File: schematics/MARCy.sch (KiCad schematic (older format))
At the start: 2 parts, among them J2 JTAG, U3 XC9572XL-TQ100

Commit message: merge from Jani's commit
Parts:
- added R?: 0.1uF, symbol Device:R_Small
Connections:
- net GND: now also R?.2
- net Vcc33: now also R?.1
- net A0: now reaches U3.32 (P32)
- net R~W: now reaches U3.33 (P33)
- net A1: now reaches U3.35 (P35)
- net ~OE: now reaches U3.36 (P36)
- net A2: now reaches U3.37 (P37)
- net A3: now reaches U3.41 (P41)
- net A4: now reaches U3.42 (P42)
- net A5: now reaches U3.49 (P49)
- net A6: now reaches U3.50 (P50)
- net A7: now reaches U3.52 (P52)
- net A8: now reaches U3.53 (P53)
- net A9: now reaches U3.54 (P54)
- net A10: now reaches U3.55 (P55)
- net A11: now reaches U3.56 (P56)
- net A12: now reaches U3.58 (P58)
- net A13: now reaches U3.59 (P59)
- net A14: now reaches U3.60 (P60)
- net A15: now reaches U3.61 (P61)
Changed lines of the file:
@@
 Connection ~ 4150 6650
 Entry Wire Line
-	5350 2050 5450 1950
-Entry Wire Line
-	5350 2150 5450 2050
-Entry Wire Line
-	5350 2250 5450 2150
-Entry Wire Line
-	5350 2350 5450 2250
-Entry Wire Line
-	5350 2450 5450 2350
-Entry Wire Line
-	5350 2550 5450 2450
-Entry Wire Line
-	5350 2650 5450 2550
-Entry Wire Line
-	5350 2750 5450 2650
-Entry Wire Line
-	5350 2850 5450 2750
-Entry Wire Line
-	5350 2950 5450 2850
-Entry Wire Line
-	5350 3050 5450 2950
-Entry Wire Line
-	5350 3150 5450 3050
-Entry Wire Line
-	5350 3250 5450 3150
-Entry Wire Line
-	5350 3350 5450 3250
-Entry Wire Line
-	5350 3450 5450 3350
-Entry Wire Line
-	5350 3550 5450 3450
-Text Label 5450 1350 0    50   ~ 10
-A[0..15]
-Text GLabel 5450 1600 2    50   Input ~ 10
-A[0..15]
-Text GLabel 2450 2050 0    50   Input ~ 10
+	5500 2050 5600 1950
+Entry Wire Line
+	5500 2150 5600 2050
+Entry Wire Line
+	5500 2250 5600 2150
+Entry Wire Line
+	5500 2350 5600 2250
+Entry Wire Line
+	5500 2450 5600 2350
+Entry Wire Line
+	5500 2550 5600 2450
+Entry Wire Line
+	5500 2650 5600 2550
+Entry Wire Line
+	5500 2750 5600 2650
+Entry Wire Line
+	5500 2850 5600 2750
+Entry Wire Line
+	5500 2950 5600 2850
+Entry Wire Line
+	5500 3050 5600 2950
+Entry Wire Line
+	5500 3150 5600 3050
+Entry Wire Line
+	5500 3250 5600 3150
+Entry Wire Line
+	5500 3350 5600 3250
+Entry Wire Line
+	5500 3450 5600 3350
+Entry Wire Line
+	5500 3550 5600 3450
+Text GLabel 2450 2050 0    50   Output ~ 10
 RTC_EN
-Text GLabel 2450 2200 0    50   Input ~ 10
+Text GLabel 2450 2200 0    50   Output ~ 10
 VIA1_EN
 Wire Wire Line
@@
 Wire Wire Line
 	3050 2150 3050 2200
-Text GLabel 2450 2350 0    50   Input ~ 10
+Text GLabel 2450 2350 0    50   Output ~ 10
 VIA2_EN
 Wire Wire Line
@@
 Wire Wire Line
 	3100 2250 3100 2350
-Text GLabel 2450 2500 0    50   Input ~ 10
+Text GLabel 2450 2500 0    50   Output ~ 10
 ROM_EN
 Wire Wire Line
@@
 Wire Wire Line
 	2600 2500 2450 2500
-Text GLabel 2450 2650 0    50   Input ~ 10
+Text GLabel 2450 2650 0    50   Output ~ 10
 RAM_EN
 Wire Wire Line
 	2650 2650 2450 2650
-Text GLabel 2450 2800 0    50   Input ~ 10
+Text GLabel 2450 2800 0    50   Output ~ 10
 UART_EN
-Text GLabel 2400 2950 0    50   Input ~ 10
+Text GLabel 2400 2950 0    50   Output ~ 10
 GRACE_EN
 Wire Wire Line
@@
 Wire Wire Line
 	2400 2950 2750 2950
-Text GLabel 2350 3100 0    50   Input ~ 10
+Text GLabel 2350 3100 0    50   Output ~ 10
 CAS
 Wire Wire Line
@@
 Wire Wire Line
 	2800 3100 2350 3100
-Text GLabel 2350 3250 0    50   Input ~ 10
+Text GLabel 2350 3250 0    50   Output ~ 10
 RAS
 Wire Wire Line
@@
 Wire Wire Line
 	2500 3250 2350 3250
-Text GLabel 2350 3400 0    50   Input ~ 10
+Text GLabel 2350 3400 0    50   Output ~ 10
 AUDIO_EN
 Wire Wire Line
@@
 Wire Wire Line
 	5950 6050 5350 6050
-Text GLabel 5400 750  2    50   Input ~ 10
-Vcc33
 Wire Wire Line
 	4650 750  5400 750
@@
 	6950 5400 5800 5400
 Entry Wire Line
-	5350 3950 5450 3850
-Entry Wire Line
-	5350 4050 5450 3950
-Entry Wire Line
-	5350 4150 5450 4050
-Entry Wire Line
-	5350 4250 5450 4150
-Entry Wire Line
-	5350 4350 5450 4250
-Entry Wire Line
-	5350 4450 5450 4350
-Entry Wire Line
-	5350 4550 5450 4450
-Entry Wire Line
-	5350 4650 5450 4550
-Entry Wire Line
-	5350 4750 5450 4650
-Entry Wire Line
-	5350 4850 5450 4750
-Entry Wire Line
-	5350 4950 5450 4850
-Entry Wire Line
-	5350 5050 5450 4950
-Text Label 5450 4100 0    50   ~ 10
+	5500 3950 5600 3850
+Entry Wire Line
+	5500 4050 5600 3950
+Entry Wire Line
+	5500 4150 5600 4050
+Entry Wire Line
+	5500 4250 5600 4150
+Entry Wire Line
+	5500 4350 5600 4250
+Entry Wire Line
+	5500 4450 5600 4350
+Entry Wire Line
+	5500 4550 5600 4450
+Entry Wire Line
+	5500 4650 5600 4550
+Entry Wire Line
+	5500 4750 5600 4650
+Entry Wire Line
+	5500 4850 5600 4750
+Entry Wire Line
+	5500 4950 5600 4850
+Entry Wire Line
+	5500 5050 5600 4950
+Text GLabel 2350 3550 0    50   Output ~ 10
+FDC_EN
+Wire Wire Line
+	3350 3350 2600 3350
+Wire Wire Line
+	2600 3350 2600 3550
+Wire Wire Line
+	2600 3550 2350 3550
+Wire Wire Line
+	5350 2050 5500 2050
+Wire Wire Line
+	5350 2150 5500 2150
+Wire Wire Line
+	5350 2250 5500 2250
+Wire Wire Line
+	5350 2350 5500 2350
+Wire Wire Line
+	5350 2450 5500 2450
+Wire Wire Line
+	5350 2550 5500 2550
+Wire Wire Line
+	5350 2650 5500 2650
+Wire Wire Line
+	5350 2750 5500 2750
+Wire Wire Line
+	5350 2850 5500 2850
+Wire Wire Line
+	5350 2950 5500 2950
+Wire Wire Line
+	5350 3050 5500 3050
+Wire Wire Line
+	5350 3150 5500 3150
+Wire Wire Line
+	5350 3250 5500 3250
+Wire Wire Line
+	5350 3350 5500 3350
+Wire Wire Line
+	5350 3450 5500 3450
+Wire Wire Line
+	5350 3550 5500 3550
+Wire Bus Line
+	5600 1950 5700 1950
+Text Label 5350 2050 0    50   ~ 0
+A0
+Text Label 5350 2150 0    50   ~ 0
+A1
+Text Label 5350 2250 0    50   ~ 0
+A2
+Text Label 5350 2350 0    50   ~ 0
+A3
+Text Label 5350 2450 0    50   ~ 0
+A4
+Text Label 5350 2550 0    50   ~ 0
+A5
+Text Label 5350 2650 0    50   ~ 0
+A6
+Text Label 5350 2750 0    50   ~ 0
+A7
+Text Label 5350 2850 0    50   ~ 0
+A8
+Text Label 5350 2950 0    50   ~ 0
+A9
+Text Label 5350 3050 0    50   ~ 0
+A10
+Text Label 5350 3150 0    50   ~ 0
+A11
+Text Label 5350 3250 0    50   ~ 0
+A12
+Text Label 5350 3350 0    50   ~ 0
+A13
+Text Label 5350 3450 0    50   ~ 0
+A14
+Text Label 5350 3550 0    50   ~ 0
+A15
+Wire Wire Line
+	5350 3950 5500 3950
+Wire Wire Line
+	5350 4050 5500 4050
+Wire Wire Line
+	5350 4150 5500 4150
+Wire Wire Line
+	5350 4250 5500 4250
+Wire Wire Line
+	5350 4350 5500 4350
+Wire Wire Line
+	5350 4450 5500 4450
+Wire Wire Line
+	5350 4550 5500 4550
+Wire Wire Line
+	5350 4650 5500 4650
+Wire Wire Line
+	5350 4750 5500 4750
+Wire Wire Line
+	5350 4850 5500 4850
+Wire Wire Line
+	5350 4950 5500 4950
+Wire Wire Line
+	5350 5050 5500 5050
+Wire Bus Line
+	5600 3850 5650 3850
+Text HLabel 5650 3850 2    50   Output ~ 0
 MA[0..11]
-Text GLabel 5450 4300 2    50   Input ~ 10
-MA[0..11]
-Text GLabel 2350 3550 0    50   Input ~ 10
-FDC_EN
-Wire Wire Line
-	3350 3350 2600 3350
-Wire Wire Line
-	2600 3350 2600 3550
-Wire Wire Line
-	2600 3550 2350 3550
+Text HLabel 5700 1950 2    50   Input ~ 0
+A[0..15]
+Text HLabel 7300 1000 0    50   Input ~ 0
+Vcc33
+$Comp
+L Device:R_Small R?
+U 1 1 5F14E0B3
+P 7450 1100
+F 0 "R?" H 7509 1146 50  0000 L CNN
+F 1 "0.1uF" H 7509 1055 50  0000 L CNN
+F 2 "" H 7450 1100 50  0001 C CNN
+F 3 "~" H 7450 1100 50  0001 C CNN
+	1    7450 1100
+	1    0    0    -1
+$EndComp
+Wire Wire Line
+	7300 1000 7450 1000
+Wire Wire Line
+	7450 1000 7800 1000
+Connection ~ 7450 1000
+Text HLabel 7300 1200 0    50   Input ~ 0
+GND
+Text GLabel 7800 1000 2    50   Output ~ 0
+Vcc33
+Text GLabel 7800 1200 2    50   Output ~ 0
+GND
+Wire Wire Line
+	7800 1200 7450 1200
+Wire Wire Line
+	7300 1200 7450 1200
+Connection ~ 7450 1200
+Text GLabel 5400 750  2    50   Input ~ 0
+Vcc33
+Text HLabel 2300 3750 0    50   Input ~ 0
+R~W
+Text HLabel 2300 3900 0    50   Output ~ 0
+~OE
+Wire Wire Line
+	3350 3450 2750 3450
+Wire Wire Line
+	2750 3450 2750 3750
+Wire Wire Line
+	2750 3750 2300 3750
+Wire Wire Line
+	3350 3550 2850 3550
+Wire Wire Line
+	2850 3550 2850 3900
+Wire Wire Line
+	2850 3900 2300 3900
 Wire Bus Line
-	5450 3850 5450 5000
+	5600 1950 5600 3450
 Wire Bus Line
-	5450 1000 5450 3600
+	5600 3850 5600 5000
 $EndSCHEMATC

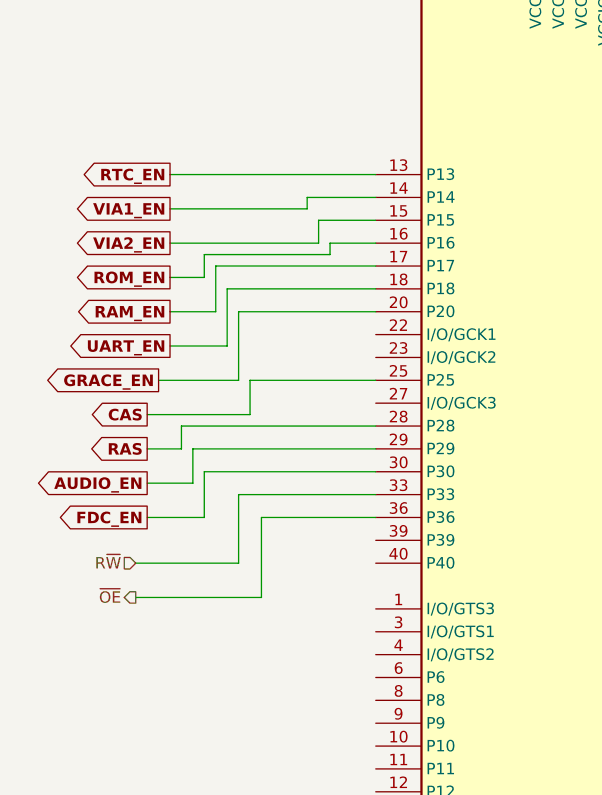
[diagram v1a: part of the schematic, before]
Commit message: Fixup heirarchial labels
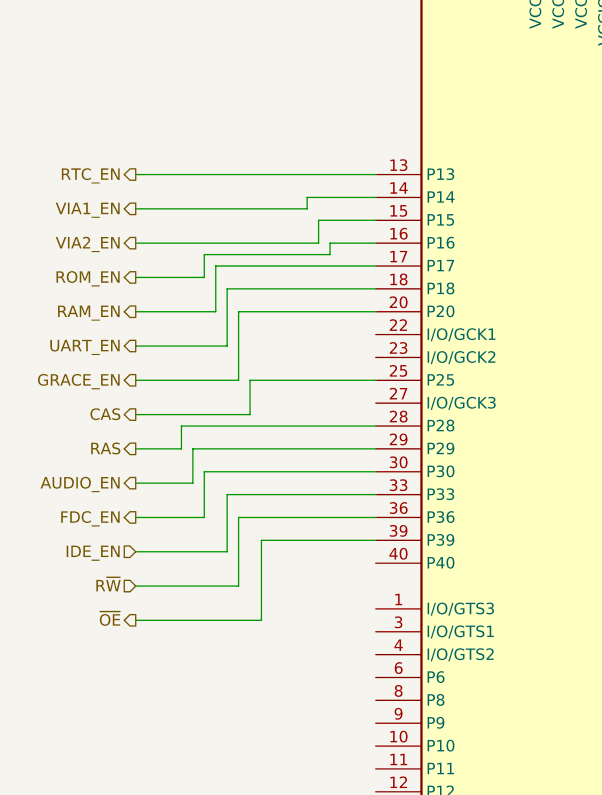
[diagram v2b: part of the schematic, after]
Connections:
- net R~W: now also U3.36 (P36); no longer U3.33 (P33)
- net ~OE: now also U3.39 (P39); no longer U3.36 (P36)
- new net IDE_EN: U3.33 (P33)
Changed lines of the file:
@@
 Entry Wire Line
 	5500 3550 5600 3450
-Text GLabel 2450 2050 0    50   Output ~ 10
-RTC_EN
-Text GLabel 2450 2200 0    50   Output ~ 10
-VIA1_EN
 Wire Wire Line
 	3350 2150 3050 2150
 Wire Wire Line
 	3050 2150 3050 2200
-Text GLabel 2450 2350 0    50   Output ~ 10
-VIA2_EN
 Wire Wire Line
 	3350 2250 3100 2250
 Wire Wire Line
 	3100 2250 3100 2350
-Text GLabel 2450 2500 0    50   Output ~ 10
-ROM_EN
 Wire Wire Line
 	3350 2350 3150 2350
@@
 	3150 2350 3150 2400
 Wire Wire Line
-	2600 2500 2450 2500
-Text GLabel 2450 2650 0    50   Output ~ 10
-RAM_EN
-Wire Wire Line
-	2650 2650 2450 2650
-Text GLabel 2450 2800 0    50   Output ~ 10
-UART_EN
-Text GLabel 2400 2950 0    50   Output ~ 10
-GRACE_EN
-Wire Wire Line
-	2450 2050 3350 2050
-Wire Wire Line
-	2450 2200 3050 2200
-Wire Wire Line
-	2450 2350 3100 2350
-Wire Wire Line
 	2600 2500 2600 2400
 Wire Wire Line
@@
 	2700 2550 3350 2550
 Wire Wire Line
-	2450 2800 2700 2800
-Wire Wire Line
 	2750 2650 2750 2950
 Wire Wire Line
 	2750 2650 3350 2650
 Wire Wire Line
-	2400 2950 2750 2950
-Text GLabel 2350 3100 0    50   Output ~ 10
-CAS
-Wire Wire Line
 	3350 2950 2800 2950
 Wire Wire Line
 	2800 2950 2800 3100
 Wire Wire Line
-	2800 3100 2350 3100
-Text GLabel 2350 3250 0    50   Output ~ 10
-RAS
-Wire Wire Line
 	3350 3150 2500 3150
 Wire Wire Line
 	2500 3150 2500 3250
 Wire Wire Line
-	2500 3250 2350 3250
-Text GLabel 2350 3400 0    50   Output ~ 10
-AUDIO_EN
-Wire Wire Line
 	3350 3250 2550 3250
 Wire Wire Line
 	2550 3250 2550 3400
-Wire Wire Line
-	2550 3400 2350 3400
 $Comp
 L Connector_Generic:Conn_02x07_Top_Bottom J2
@@
 Entry Wire Line
 	5500 5050 5600 4950
-Text GLabel 2350 3550 0    50   Output ~ 10
-FDC_EN
 Wire Wire Line
 	3350 3350 2600 3350
 Wire Wire Line
 	2600 3350 2600 3550
-Wire Wire Line
-	2600 3550 2350 3550
 Wire Wire Line
 	5350 2050 5500 2050
@@
 Text GLabel 5400 750  2    50   Input ~ 0
 Vcc33
-Text HLabel 2300 3750 0    50   Input ~ 0
+Text HLabel 2300 3850 0    50   Input ~ 0
 R~W
-Text HLabel 2300 3900 0    50   Output ~ 0
+Text HLabel 2300 4000 0    50   Output ~ 0
 ~OE
 Wire Wire Line
-	3350 3450 2750 3450
-Wire Wire Line
-	2750 3450 2750 3750
-Wire Wire Line
-	2750 3750 2300 3750
-Wire Wire Line
-	3350 3550 2850 3550
-Wire Wire Line
-	2850 3550 2850 3900
-Wire Wire Line
-	2850 3900 2300 3900
+	2750 3550 2750 3850
+Wire Wire Line
+	2750 3850 2300 3850
+Wire Wire Line
+	2850 3650 2850 4000
+Wire Wire Line
+	2850 4000 2300 4000
+Text HLabel 2300 2050 0    50   Output ~ 0
+RTC_EN
+Text HLabel 2300 2200 0    50   Output ~ 0
+VIA1_EN
+Text HLabel 2300 2350 0    50   Output ~ 0
+VIA2_EN
+Text HLabel 2300 2500 0    50   Output ~ 0
+ROM_EN
+Text HLabel 2300 2650 0    50   Output ~ 0
+RAM_EN
+Text HLabel 2300 2800 0    50   Output ~ 0
+UART_EN
+Text HLabel 2300 2950 0    50   Output ~ 0
+GRACE_EN
+Text HLabel 2300 3400 0    50   Output ~ 0
+AUDIO_EN
+Text HLabel 2300 3550 0    50   Output ~ 0
+FDC_EN
+Text HLabel 2300 3100 0    50   Output ~ 0
+CAS
+Text HLabel 2300 3250 0    50   Output ~ 0
+RAS
+Wire Wire Line
+	2300 2050 3350 2050
+Wire Wire Line
+	2300 2200 3050 2200
+Wire Wire Line
+	2300 2350 3100 2350
+Wire Wire Line
+	2300 2500 2600 2500
+Wire Wire Line
+	2300 2650 2650 2650
+Wire Wire Line
+	2300 2800 2700 2800
+Wire Wire Line
+	2300 2950 2750 2950
+Wire Wire Line
+	2300 3100 2800 3100
+Wire Wire Line
+	2300 3250 2500 3250
+Wire Wire Line
+	2300 3400 2550 3400
+Wire Wire Line
+	2300 3550 2600 3550
+Text HLabel 2300 3700 0    50   Input ~ 0
+IDE_EN
+Wire Wire Line
+	3350 3650 2850 3650
+Wire Wire Line
+	2750 3550 3350 3550
+Wire Wire Line
+	2700 3450 3350 3450
+Wire Wire Line
+	2700 3450 2700 3700
+Wire Wire Line
+	2700 3700 2300 3700
 Wire Bus Line
 	5600 1950 5600 3450

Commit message: Added missing IDE control signals for the latches, bus drivers, reads/writes and chip selects.
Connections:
- net IDE_CS0: now reaches U3.10 (P10)
- net IDE_CS1: now reaches U3.11 (P11)
- net IOR: now reaches U3.12 (P12)
- net IDE_LDR: now reaches U3.40 (P40)
- net IDE_UDR: now reaches U3.6 (P6)
- net IDE_LDW: now reaches U3.8 (P8)
- net IOW: now reaches U3.87 (P87)
- net IDE_UDW: now reaches U3.9 (P9)
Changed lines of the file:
@@
 Wire Wire Line
 	2700 3700 2300 3700
+Text GLabel 2450 4150 0    50   Input ~ 0
+IDE_LDR
+Text GLabel 2450 4300 0    50   Input ~ 0
+IDE_UDR
+Text GLabel 2450 4450 0    50   Input ~ 0
+IDE_LDW
+Text GLabel 2450 4600 0    50   Input ~ 0
+IDE_UDW
+Text GLabel 2450 4750 0    50   Input ~ 0
+IDE_CS0
+Text GLabel 2450 4900 0    50   Input ~ 0
+IDE_CS1
+Wire Wire Line
+	3350 3750 2900 3750
+Wire Wire Line
+	2900 3750 2900 4150
+Wire Wire Line
+	2900 4150 2450 4150
+Wire Wire Line
+	3350 4250 2700 4250
+Wire Wire Line
+	2700 4250 2700 4300
+Wire Wire Line
+	2700 4300 2450 4300
+Wire Wire Line
+	3350 4350 2700 4350
+Wire Wire Line
+	2700 4350 2700 4450
+Wire Wire Line
+	2700 4450 2450 4450
+Wire Wire Line
+	3350 4450 2750 4450
+Wire Wire Line
+	2750 4450 2750 4600
+Wire Wire Line
+	2750 4600 2450 4600
+Wire Wire Line
+	2800 4550 2800 4750
+Wire Wire Line
+	2800 4750 2450 4750
+Wire Wire Line
+	2850 4650 2850 4900
+Wire Wire Line
+	2850 4900 2450 4900
+Wire Wire Line
+	2850 4650 3350 4650
+Wire Wire Line
+	2800 4550 3350 4550
+Text GLabel 2400 5050 0    50   Input ~ 0
+IOR
+Text GLabel 2400 5200 0    50   Input ~ 0
+IOW
+Wire Wire Line
+	3350 4750 2900 4750
+Wire Wire Line
+	2900 4750 2900 5050
+Wire Wire Line
+	2900 5050 2400 5050
+Wire Wire Line
+	3350 4850 2950 4850
+Wire Wire Line
+	2950 4850 2950 5200
+Wire Wire Line
+	2950 5200 2400 5200
 Wire Bus Line
 	5600 1950 5600 3450

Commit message: Added missing FDC control signals.
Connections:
- net FDC_SIDE: now reaches U3.91 (P91)
- net FDC_MTREN: now reaches U3.92 (P92)
- net FDC_DRVA: now reaches U3.93 (P93)
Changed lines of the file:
@@
 Wire Wire Line
 	2950 5200 2400 5200
+Text GLabel 2350 5350 0    50   Input ~ 0
+FDC_SIDE
+Text GLabel 2350 5500 0    50   Input ~ 0
+FDC_MTREN
+Text GLabel 2350 5650 0    50   Input ~ 0
+FDC_DRVA
+Wire Wire Line
+	3350 4950 3000 4950
+Wire Wire Line
+	3000 4950 3000 5350
+Wire Wire Line
+	3000 5350 2350 5350
+Wire Wire Line
+	3050 5050 3050 5500
+Wire Wire Line
+	3050 5500 2350 5500
+Wire Wire Line
+	3050 5050 3350 5050
+Wire Wire Line
+	3350 5150 3100 5150
+Wire Wire Line
+	3100 5150 3100 5650
+Wire Wire Line
+	3100 5650 2350 5650
 Wire Bus Line
 	5600 1950 5600 3450

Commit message: Fixes to FDC signal mapping.
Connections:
- net FDC_DRVA: no longer names the net of U3.93 (P93)
- net FDC_MTREN: no longer names the net of U3.92 (P92)
- net FDC_SIDE: no longer names the net of U3.91 (P91)
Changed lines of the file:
@@
 Wire Wire Line
 	2950 5200 2400 5200
-Text GLabel 2350 5350 0    50   Input ~ 0
-FDC_SIDE
-Text GLabel 2350 5500 0    50   Input ~ 0
-FDC_MTREN
-Text GLabel 2350 5650 0    50   Input ~ 0
-FDC_DRVA
-Wire Wire Line
-	3350 4950 3000 4950
-Wire Wire Line
-	3000 4950 3000 5350
-Wire Wire Line
-	3000 5350 2350 5350
-Wire Wire Line
-	3050 5050 3050 5500
-Wire Wire Line
-	3050 5500 2350 5500
-Wire Wire Line
-	3050 5050 3350 5050
-Wire Wire Line
-	3350 5150 3100 5150
-Wire Wire Line
-	3100 5150 3100 5650
-Wire Wire Line
-	3100 5650 2350 5650
 Wire Bus Line
 	5600 1950 5600 3450
